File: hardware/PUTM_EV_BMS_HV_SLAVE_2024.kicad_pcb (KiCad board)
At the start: 4 copper layers, 105 x 48 mm, 186 parts, among them CN1 4x100nF, CN2 4x100nF, CN3 4x100nF, CN4 4x100nF, CN5 4x100nF, CN6 4x100nF, CN7 4x100nF, CN8 4x100nF, IC1 LTC6804HG-1#PBF, IC2 LTC6804HG-1#PBF, J1 TST-110-01-T-D, J2 TST-110-01-T-D, J3 M80-5100442, J4 M80-5100442, J5 Conn_01x01_Pin, J6 Conn_01x01_Pin, Q1 BCP56, Q10 CPH3351, Q11 CPH3351, Q12 BCP56, Q13 CPH3351, Q14 CPH3351, Q15 CPH3351, Q16 CPH3351, Q17 CPH3351, Q18 CPH3351, Q19 CPH3351, Q2 CPH3351, Q20 CPH3351, Q21 CPH3351, Q22 CPH3351, Q3 CPH3351, Q4 CPH3351, Q5 CPH3351, Q6 CPH3351, Q7 CPH3351, Q8 CPH3351, Q9 CPH3351, T1 HM1236NL, T3 HM1236NL

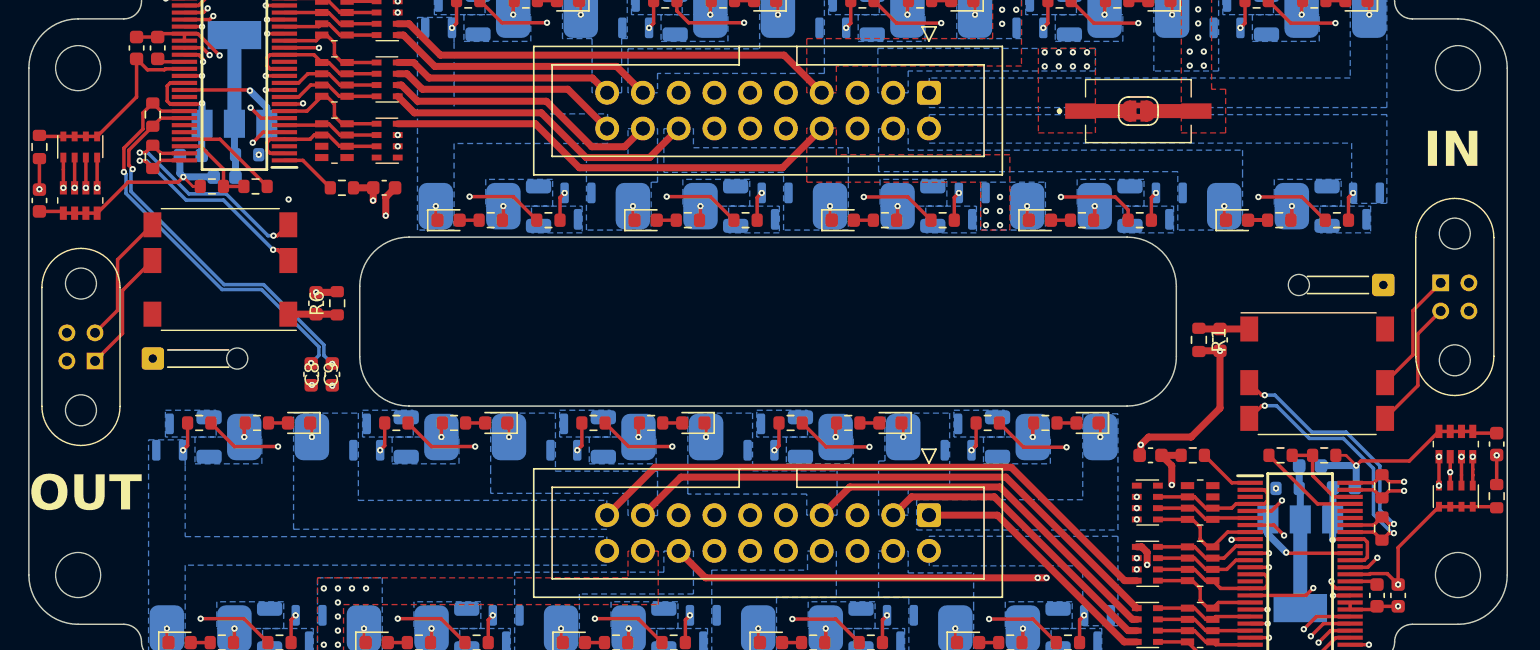
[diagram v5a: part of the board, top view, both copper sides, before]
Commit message: added temp disconnect, beautify schematic
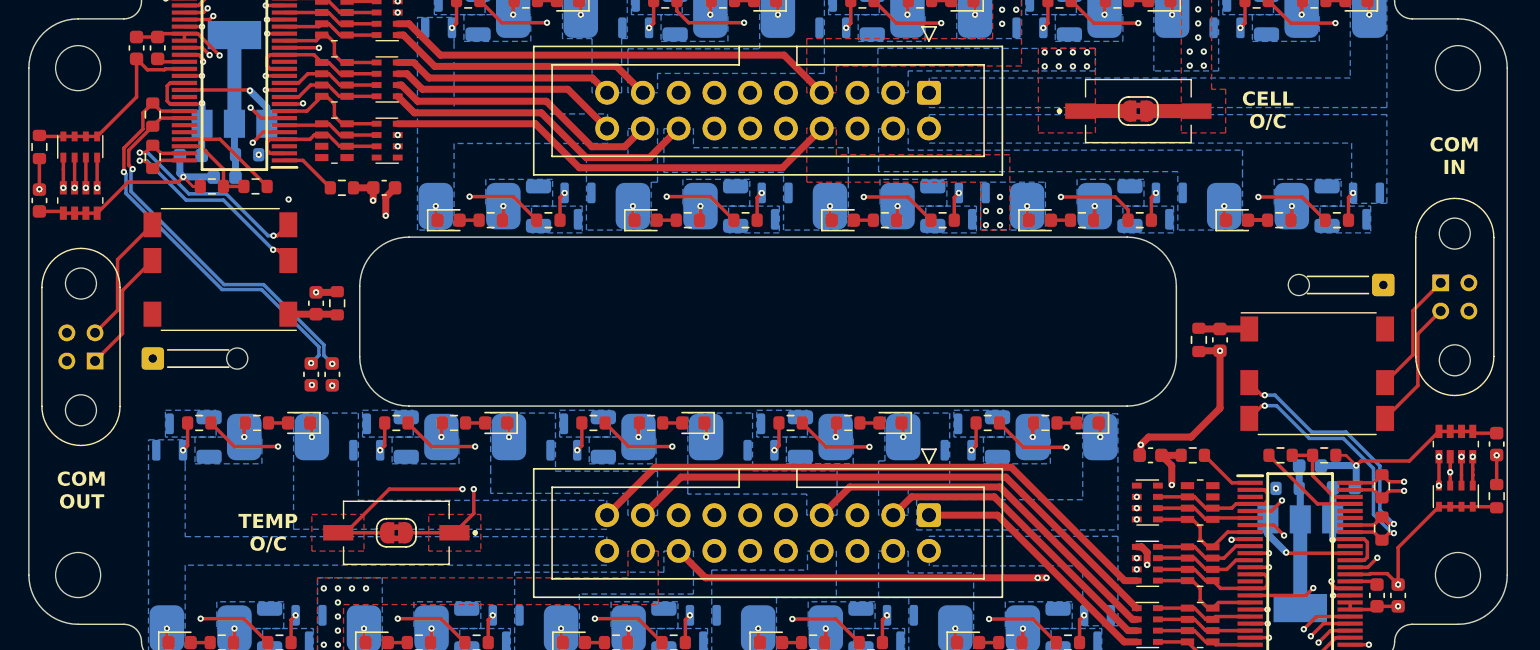
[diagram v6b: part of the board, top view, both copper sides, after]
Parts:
- added JP2: MES, Jumper:SolderJumper-2_P1.3mm_Bridged2Bar_RoundedPad1.0x1.5mm, F.Cu at (151.1, 89.0)
- added S2: A6SN-1104, Samacsys:A6SN1104, F.Cu at (151.1, 89.0)
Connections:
- CN7 pad 7: /TH3+ -> /TH3_SW+
- IC1 pad 29: /TH3+ -> /TH3_SW+
- RN7 pad 2: /TH3+ -> /TH3_SW+
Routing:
- net /TH3_SW+: track 0.00 -> 120.0 mm, vias 0 -> 3
- net /TH3+: track 86.1 -> 25.0 mm, vias 2 -> 1
- added copper zone on F.Cu, net /TH3+
- added copper zone on F.Cu, net /TH3_SW+
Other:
- board text added: "CELL O/C"
- board text added: "COM IN"
- board text added: "COM OUT"
- board text added: "TEMP O/C"
- board text removed: "IN"
- board text removed: "OUT"

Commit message: replaced signal transformer with rated capacitors, made the design more general for future use
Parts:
- removed H1, H2, H3, H4: MountingHole, MountingHole:MountingHole_3.2mm_M3
- removed J5, J6: Conn_01x01_Pin, Connector_Wire:SolderWire-0.1sqmm_1x01_D0.4mm_OD1mm_Relief
- removed R11, R15, R19, R23, R27, R31, R35, R39, R43, R47, R61, R65, R69, R73, R77, R81, R85, R89, R93, R97: 3.3k, Resistor_SMD:R_0603_1608Metric
- removed T1, T3: HM1236NL, Samacsys:HM1236NL
- added C10: 10nF/1kV, Capacitor_SMD:C_1206_3216Metric, F.Cu at (189.5, 5.10)
- added C11: 10nF/1kV, Capacitor_SMD:C_1206_3216Metric, F.Cu at (189.5, 8.45)
- added C12: 10nF/1kV, Capacitor_SMD:C_1206_3216Metric, F.Cu at (85.8, 90.5)
- added C13: 10nF/1kV, Capacitor_SMD:C_1206_3216Metric, F.Cu at (85.8, 93.9)
- added D21: LED, LED_SMD:LED_0603_1608Metric, F.Cu at (82.9, 115.4)
- added D22: LED, LED_SMD:LED_0603_1608Metric, F.Cu at (177.7, -1.36)
- added D23: LED, LED_SMD:LED_0603_1608Metric, F.Cu at (82.9, 118.0)
- added D24: LED, LED_SMD:LED_0603_1608Metric, F.Cu at (165.8, 12.6)
- added F21: 1206L600SLWR, Fuse:Fuse_2512_6332Metric, B.Cu at (39.0, 91.3)
- added F22: 1206L600SLWR, Fuse:Fuse_2512_6332Metric, F.Cu at (178.2, -4.18)
- added F23: 1206L600SLWR, Fuse:Fuse_2512_6332Metric, B.Cu at (39.0, 96.2)
- added F24: 1206L600SLWR, Fuse:Fuse_2512_6332Metric, F.Cu at (166.3, 9.80)
- added Q23: CPH3351, Package_TO_SOT_SMD:SOT-23, F.Cu at (90.2, 78.6)
- added Q24: CPH3351, Package_TO_SOT_SMD:SOT-23, F.Cu at (183.2, -3.30)
- added Q25: CPH3351, Package_TO_SOT_SMD:SOT-23, F.Cu at (90.2, 83.2)
- added Q26: CPH3351, Package_TO_SOT_SMD:SOT-23, F.Cu at (171.2, 10.7)
- added R24: 15/2W, Resistor_SMD:R_2512_6332Metric, F.Cu at (180.1, -8.13)
- added R36: 330, Resistor_SMD:R_0603_1608Metric, F.Cu at (182.7, 0.17)
- added R44: 15/2W, Resistor_SMD:R_2512_6332Metric, B.Cu at (56.4, 96.2)
- added R48: 330, Resistor_SMD:R_0603_1608Metric, F.Cu at (70.7, 111.4)
- added R50: 15/2W, Resistor_SMD:R_2512_6332Metric, F.Cu at (168.2, 5.85)
- added R55: 330, Resistor_SMD:R_0603_1608Metric, F.Cu at (170.8, 14.2)
- added R57: 100, Resistor_SMD:R_0603_1608Metric, F.Cu at (70.7, 113.9)
- added R58: 100, Resistor_SMD:R_0603_1608Metric, F.Cu at (180.2, -13.8)
- added RN10: 4x3.3k, Resistor_SMD:R_Array_Convex_4x0603, F.Cu at (180.3, -17.4)
- added RN11: 4x3.3k, Resistor_SMD:R_Array_Convex_4x0603, F.Cu at (89.2, 73.8)
- added RN12: 4x3.3k, Resistor_SMD:R_Array_Convex_4x0603, F.Cu at (184.4, -17.4)
- added RN13: 4x3.3k, Resistor_SMD:R_Array_Convex_4x0603, F.Cu at (93.4, 73.8)
- added RN14: 4x3.3k, Resistor_SMD:R_Array_Convex_4x0603, F.Cu at (188.6, -17.4)
- added RN9: 4x3.3k, Resistor_SMD:R_Array_Convex_4x0603, F.Cu at (85.1, 73.8)
- C18, C3, Q2, Q3, R5: moved to F.Cu
- C6, C7: value 10nF -> 10nF/1kV; footprint Capacitor_SMD:C_0603_1608Metric -> Capacitor_SMD:C_1206_3216Metric
- C8, C9: value 10nF/50V -> 10nF/1kV; footprint Capacitor_SMD:C_0603_1608Metric -> Capacitor_SMD:C_1206_3216Metric
- F1, F10, F11, F12, F13, F14, F15, F16, F17, F18, F19, F2, F20, F3, F4, F5, F6, F7, F8, F9: footprint Samacsys:1206L075SLYR -> Fuse:Fuse_2512_6332Metric
- J1, J2: footprint Connector_IDC:IDC-Header_2x10_P2.54mm_Vertical -> Connector_IDC:IDC-Header_2x10_P2.54mm_Latch6.5mm_Vertical
- R1: value 10k -> 15/2W; footprint Resistor_SMD:R_0603_1608Metric -> Resistor_SMD:R_2512_6332Metric; moved to B.Cu
- R13, R17, R21, R25, R29, R33, R37, R41, R45, R59, R63, R67, R71, R75, R79, R83, R87, R9, R91, R95: footprint Samacsys:RESC6331X80N -> Resistor_SMD:R_2512_6332Metric
- R6: value 10k -> 330
- RN1, RN2, RN3, RN4, RN5, RN6: footprint Samacsys:EXBV8V101JV -> Resistor_SMD:R_Array_Convex_4x0603
- moved RN7 190.9 mm to (37.8, 115.9)
- moved D1 183.7 mm to (22.0, 126.0), turned to 0 degrees
- moved R9 181.8 mm to (22.0, 125.0), turned to -90 degrees
- moved F1 180.9 mm to (18.0, 125.0)
- moved R10 180.3 mm to (22.0, 124.0)
- moved D2 178.8 mm to (10.2, 112.5)
- moved Q2 178.2 mm to (18.0, 125.0), turned to 0 degrees
- moved R14 176.3 mm to (10.2, 115.0)
- moved Q3 173.9 mm to (5.95, 113.6)
- moved R13 166.4 mm to (22.0, 117.0), turned to -90 degrees
- moved F2 165.5 mm to (18.0, 117.0)
- moved D3 164.7 mm to (8.90, 102.9)
- moved C4 163.3 mm to (67.0, 100.6)
- moved R18 162.1 mm to (8.90, 105.5)
- moved R2 160.4 mm to (69.5, 100.6)
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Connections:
- C19 pad 1: /C10+ -> /L_LTC/V+
- C20 pad 1: /C20+ -> /R_LTC/V+
- C6 pad 1: Net-(C6-Pad1) -> /OUT+
- C6 pad 2: /C11- -> /IPB
- C7 pad 1: /C1- -> /OUT-
- C7 pad 2: Net-(C7-Pad2) -> /IMB
- C8 pad 1: /L_LTC/IPB -> Net-(J3-Pin_3)
- C8 pad 2: /R_LTC/IPA -> /C11-
- C9 pad 1: /R_LTC/IMA -> /IPA
- C9 pad 2: /L_LTC/IMB -> /IN+
- CN1 pad 1: /L_LTC/C3 -> /L_LTC/C1
- CN1 pad 3: /L_LTC/C1 -> /L_LTC/C3
- CN1 pad 4: /L_LTC/C0 -> /L_LTC/C4
- CN1 pad 5: /L_LTC/C1 -> /L_LTC/C3
- CN1 pad 7: /L_LTC/C3 -> /L_LTC/C1
- CN1 pad 8: /L_LTC/C4 -> /L_LTC/C0
- CN2 pad 1: /R_LTC/C3 -> /R_LTC/C1
- CN2 pad 3: /R_LTC/C1 -> /R_LTC/C3
- CN2 pad 4: /R_LTC/C0 -> /R_LTC/C4
- CN2 pad 5: /R_LTC/C1 -> /R_LTC/C3
- CN2 pad 7: /R_LTC/C3 -> /R_LTC/C1
- CN2 pad 8: /R_LTC/C4 -> /R_LTC/C0
- CN3 pad 1: /L_LTC/C8 -> /L_LTC/C5
- CN3 pad 2: /L_LTC/C7 -> /L_LTC/C6
- CN3 pad 3: /L_LTC/C5 -> /L_LTC/C7
- CN3 pad 4: /L_LTC/C4 -> /L_LTC/C8
- CN3 pad 5: /L_LTC/C5 -> /L_LTC/C7
- CN3 pad 6: /L_LTC/C7 -> /L_LTC/C6
- CN3 pad 7: /L_LTC/C8 -> /L_LTC/C5
- CN3 pad 8: /L_LTC/C9 -> /L_LTC/C4
- CN4 pad 1: /R_LTC/C8 -> /R_LTC/C5
- CN4 pad 2: /R_LTC/C7 -> /R_LTC/C6
- CN4 pad 3: /R_LTC/C5 -> /R_LTC/C7
- CN4 pad 4: /R_LTC/C4 -> /R_LTC/C8
- CN4 pad 5: /R_LTC/C5 -> /R_LTC/C7
- CN4 pad 6: /R_LTC/C7 -> /R_LTC/C6
- CN4 pad 7: /R_LTC/C8 -> /R_LTC/C5
- CN4 pad 8: /R_LTC/C9 -> /R_LTC/C4
- CN5 pad 1: unconnected-(CN5-R1.1-Pad1) -> /L_LTC/C9
- CN5 pad 2: /L_LTC/C11 -> /L_LTC/C10
- CN5 pad 3: /L_LTC/C10 -> /L_LTC/C11
- CN5 pad 4: /L_LTC/C9 -> /L_LTC/C12
- CN5 pad 5: /L_LTC/C10 -> /L_LTC/C11
- CN5 pad 6: /L_LTC/C11 -> /L_LTC/C10
- CN5 pad 7: unconnected-(CN5-R2.2-Pad7) -> /L_LTC/C9
- CN5 pad 8: unconnected-(CN5-R1.2-Pad8) -> /L_LTC/C8
- CN6 pad 1: unconnected-(CN6-R1.1-Pad1) -> /R_LTC/C9
- CN6 pad 2: /R_LTC/C11 -> /R_LTC/C10
- CN6 pad 3: /R_LTC/C10 -> /R_LTC/C11
- CN6 pad 4: /R_LTC/C9 -> /R_LTC/C12
- CN6 pad 5: /R_LTC/C10 -> /R_LTC/C11
- CN6 pad 6: /R_LTC/C11 -> /R_LTC/C10
- CN6 pad 7: unconnected-(CN6-R2.2-Pad7) -> /R_LTC/C9
- CN6 pad 8: unconnected-(CN6-R1.2-Pad8) -> /R_LTC/C8
- IC1 pad 14: /L_LTC/C5 -> /L_LTC/C6
- IC1 pad 2: /L_LTC/C11 -> /L_LTC/C12
- IC2 pad 14: /R_LTC/C5 -> /R_LTC/C6
- IC2 pad 2: /R_LTC/C11 -> /R_LTC/C12
- JP1 pad 1: /C11+ -> Net-(JP1-A)
- JP1 pad 2: /C11_SW+ -> Net-(JP1-B)
- JP2 pad 1: /TH3+ -> Net-(JP2-A)
- JP2 pad 2: /TH3_SW+ -> Net-(JP2-B)
- Q10 pad 1: Net-(Q10-G) -> /L_LTC/DCH9/S
- Q11 pad 1: Net-(Q11-G) -> /L_LTC/DCH10/S
- Q13 pad 1: Net-(Q13-G) -> /R_LTC/DCH5/S
- Q14 pad 1: Net-(Q14-G) -> /R_LTC/DCH9/S
- Q15 pad 1: Net-(Q15-G) -> /R_LTC/DCH10/S
- Q16 pad 1: Net-(Q16-G) -> /R_LTC/DCH1/S
- Q17 pad 1: Net-(Q17-G) -> /R_LTC/DCH6/S
- Q18 pad 1: Net-(Q18-G) -> /R_LTC/DCH3/S
- Q19 pad 1: Net-(Q19-G) -> /R_LTC/DCH2/S
- Q2 pad 1: Net-(Q2-G) -> /L_LTC/DCH1/S
- Q20 pad 1: Net-(Q20-G) -> /R_LTC/DCH4/S
- Q21 pad 1: Net-(Q21-G) -> /R_LTC/DCH8/S
- Q22 pad 1: Net-(Q22-G) -> /R_LTC/DCH7/S
- Q3 pad 1: Net-(Q3-G) -> /L_LTC/DCH2/S
- Q4 pad 1: Net-(Q4-G) -> /L_LTC/DCH3/S
- Q5 pad 1: Net-(Q5-G) -> /L_LTC/DCH4/S
- Q6 pad 1: Net-(Q6-G) -> /L_LTC/DCH5/S
- Q7 pad 1: Net-(Q7-G) -> /L_LTC/DCH6/S
- Q8 pad 1: Net-(Q8-G) -> /L_LTC/DCH7/S
- Q9 pad 1: Net-(Q9-G) -> /L_LTC/DCH8/S
- R1 pad 1: Net-(C7-Pad2) -> Net-(F21-Pad1)
- R1 pad 2: /C1- -> /C10+
- R4 pad 2: /C10+ -> /L_LTC/V+
- R5 pad 1: /C10+ -> /L_LTC/V+
- R51 pad 2: /C20+ -> /R_LTC/V+
- R53 pad 1: /C20+ -> /R_LTC/V+
- R6 pad 1: Net-(C6-Pad1) -> Net-(F21-Pad1)
- R6 pad 2: /C11- -> Net-(D21-A)
- RN1 pad 1: /C3+ -> /L_LTC/C5
- RN1 pad 2: /C2+ -> /L_LTC/C6
- RN1 pad 3: /C1+ -> /L_LTC/C7
- RN1 pad 4: /C1- -> /L_LTC/C8
- RN1 pad 5: /L_LTC/C0 -> /C8+
- RN1 pad 6: /L_LTC/C1 -> /C7+
- RN1 pad 7: /L_LTC/C2 -> /C6+
- RN1 pad 8: /L_LTC/C3 -> /C5+
- RN2 pad 1: /C13+ -> /R_LTC/C5
- RN2 pad 2: /C12+ -> /R_LTC/C6
- RN2 pad 3: /C11_SW+ -> /R_LTC/C7
- RN2 pad 4: /C11- -> /R_LTC/C8
- RN2 pad 5: /R_LTC/C0 -> /C18+
- RN2 pad 6: /R_LTC/C1 -> /C17+
- RN2 pad 7: /R_LTC/C2 -> /C16+
- RN2 pad 8: /R_LTC/C3 -> /C15+
- RN3 pad 1: /C7+ -> /L_LTC/C1
- RN3 pad 2: /C6+ -> /L_LTC/C2
- RN3 pad 3: /C5+ -> /L_LTC/C3
- RN3 pad 4: /C4+ -> /L_LTC/C4
- RN3 pad 5: /L_LTC/C4 -> /C4+
- RN3 pad 6: /L_LTC/C5 -> /C3+
- RN3 pad 7: /L_LTC/C7 -> /C2+
- RN3 pad 8: /L_LTC/C8 -> /C1+
- RN4 pad 1: /C17+ -> /R_LTC/C1
- RN4 pad 2: /C16+ -> /R_LTC/C2
- RN4 pad 3: /C15+ -> /R_LTC/C3
- RN4 pad 4: /C14+ -> /R_LTC/C4
- RN4 pad 5: /R_LTC/C4 -> /C14+
- RN4 pad 6: /R_LTC/C5 -> /C13+
- RN4 pad 7: /R_LTC/C7 -> /C12+
- RN4 pad 8: /R_LTC/C8 -> /C11_SW+
- RN5 pad 1: unconnected-(RN5-R1.1-Pad1) -> /L_LTC/C9
- RN5 pad 2: /C10+ -> /L_LTC/C10
- RN5 pad 3: /C9+ -> /L_LTC/C11
- RN5 pad 4: /C8+ -> /L_LTC/C12
- RN5 pad 5: /L_LTC/C9 -> /L_LTC/V+
- RN5 pad 6: /L_LTC/C10 -> /L_LTC/C11+
- RN5 pad 7: /L_LTC/C11 -> /C10+
- RN5 pad 8: unconnected-(RN5-R1.2-Pad8) -> /C9+
- RN6 pad 1: unconnected-(RN6-R1.1-Pad1) -> /R_LTC/C9
- RN6 pad 2: /C20+ -> /R_LTC/C10
- RN6 pad 3: /C19+ -> /R_LTC/C11
- RN6 pad 4: /C18+ -> /R_LTC/C12
- RN6 pad 5: /R_LTC/C9 -> /R_LTC/V+
- RN6 pad 6: /R_LTC/C10 -> /R_LTC/C11+
- RN6 pad 7: /R_LTC/C11 -> /C20+
- RN6 pad 8: unconnected-(RN6-R1.2-Pad8) -> /C19+
- S1 pad 1: /C11+ -> Net-(JP1-A)
- S1 pad 2: /C11_SW+ -> Net-(JP1-B)
- S2 pad 1: /TH3+ -> Net-(JP2-A)
- S2 pad 2: /TH3_SW+ -> Net-(JP2-B)
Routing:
- net /C11-: track 139.6 -> 0.00 mm, vias 8 -> 0
- net /TH3_SW+: track 120.0 -> 0.00 mm, vias 3 -> 0
- net /C1-: track 116.7 -> 0.00 mm, vias 6 -> 0
- net /R_LTC/S1: track 95.4 -> 0.00 mm, vias 2 -> 0
- net /L_LTC/S5: track 90.9 -> 0.00 mm, vias 2 -> 0
- net /TH6+: track 87.7 -> 0.00 mm, vias 2 -> 0
- net /L_LTC/S7: track 86.5 -> 0.00 mm, vias 2 -> 0
- net /TH1+: track 86.1 -> 0.00 mm, vias 2 -> 0
- net /TH8+: track 85.8 -> 0.00 mm, vias 2 -> 0
- net /L_LTC/IMB: track 85.7 -> 0.00 mm, vias 2 -> 0
- net /L_LTC/IPB: track 84.7 -> 0.00 mm, vias 2 -> 0
- net /L_LTC/S4: track 83.4 -> 0.00 mm, vias 2 -> 0
- net /TH7+: track 83.1 -> 0.00 mm, vias 2 -> 0
- net /TH2+: track 82.8 -> 0.00 mm, vias 2 -> 0
- net /R_LTC/S11: track 81.0 -> 0.00 mm, vias 2 -> 0
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- removed copper zone on B.Cu, net /C1+
- removed copper zone on B.Cu, net /C1-
- removed copper zone on B.Cu, net /C10+
- removed copper zone on B.Cu, net /C11+
- removed copper zone on F.Cu, net /C11+
- removed copper zone on B.Cu, net /C11-
- removed copper zone on B.Cu, net /C11_SW+
- removed copper zone on F.Cu, net /C11_SW+
- removed copper zone on B.Cu, net /C12+
- removed copper zone on F.Cu, net /C12+
- removed copper zone on B.Cu, net /C13+
- removed copper zone on B.Cu, net /C14+
- removed copper zone on B.Cu, net /C15+
- removed copper zone on B.Cu, net /C16+
- removed copper zone on B.Cu, net /C17+
- removed copper zone on B.Cu, net /C18+
- removed copper zone on F.Cu, net /C18+
- removed copper zone on B.Cu, net /C19+
- removed copper zone on B.Cu, net /C2+
- removed copper zone on B.Cu, net /C20+
- removed copper zone on B.Cu, net /C3+
- removed copper zone on B.Cu, net /C4+
- removed copper zone on B.Cu, net /C5+
- removed copper zone on B.Cu, net /C6+
- removed copper zone on F.Cu, net /C6+
- removed copper zone on B.Cu, net /C7+
- removed copper zone on B.Cu, net /C8+
- removed copper zone on B.Cu, net /C9+
- removed copper zone on F.Cu, net /TH3+
- removed copper zone on F.Cu, net /TH3_SW+
- removed copper zone on B.Cu, net Net-(F1-Pad1)
- removed copper zone on B.Cu, net Net-(F10-Pad1)
- removed copper zone on B.Cu, net Net-(F11-Pad1)
- removed copper zone on B.Cu, net Net-(F12-Pad1)
- removed copper zone on B.Cu, net Net-(F13-Pad1)
- removed copper zone on B.Cu, net Net-(F14-Pad1)
- removed copper zone on B.Cu, net Net-(F15-Pad1)
- removed copper zone on B.Cu, net Net-(F16-Pad1)
- removed copper zone on B.Cu, net Net-(F17-Pad1)
- removed copper zone on B.Cu, net Net-(F18-Pad1)
- removed copper zone on B.Cu, net Net-(F19-Pad1)
- removed copper zone on B.Cu, net Net-(F2-Pad1)
- removed copper zone on B.Cu, net Net-(F20-Pad1)
- removed copper zone on B.Cu, net Net-(F3-Pad1)
- removed copper zone on B.Cu, net Net-(F4-Pad1)
- removed copper zone on B.Cu, net Net-(F5-Pad1)
- removed copper zone on B.Cu, net Net-(F6-Pad1)
- removed copper zone on B.Cu, net Net-(F7-Pad1)
- removed copper zone on B.Cu, net Net-(F8-Pad1)
- removed copper zone on B.Cu, net Net-(F9-Pad1)
- removed copper zone on B.Cu, net Net-(Q10-D)
- removed copper zone on B.Cu, net Net-(Q11-D)
- removed copper zone on B.Cu, net Net-(Q13-D)
- removed copper zone on B.Cu, net Net-(Q14-D)
- removed copper zone on B.Cu, net Net-(Q15-D)
- removed copper zone on B.Cu, net Net-(Q16-D)
- removed copper zone on B.Cu, net Net-(Q17-D)
- removed copper zone on B.Cu, net Net-(Q18-D)
- removed copper zone on B.Cu, net Net-(Q19-D)
- removed copper zone on B.Cu, net Net-(Q2-D)
- removed copper zone on B.Cu, net Net-(Q20-D)
- removed copper zone on B.Cu, net Net-(Q21-D)
- removed copper zone on B.Cu, net Net-(Q22-D)
- removed copper zone on B.Cu, net Net-(Q3-D)
- removed copper zone on B.Cu, net Net-(Q4-D)
- removed copper zone on B.Cu, net Net-(Q5-D)
- removed copper zone on B.Cu, net Net-(Q6-D)
- removed copper zone on B.Cu, net Net-(Q7-D)
- removed copper zone on B.Cu, net Net-(Q8-D)
- removed copper zone on B.Cu, net Net-(Q9-D)
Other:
- board size 105 x 48 mm -> 281.2 x 199.9 mm
